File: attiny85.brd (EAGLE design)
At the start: 88.3 x 50.2 mm, 9 parts, among them U2 ATTINY85V-10SU

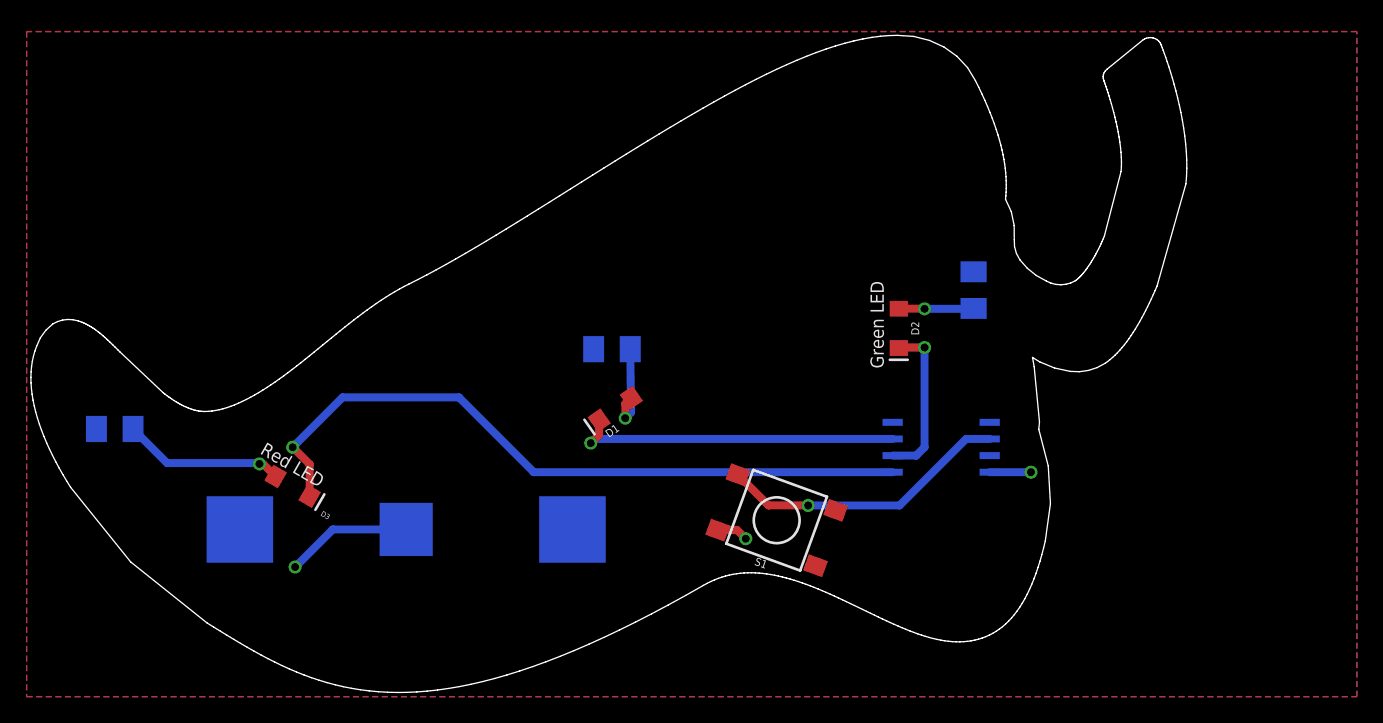
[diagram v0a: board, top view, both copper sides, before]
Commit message: Flipping to output through the attiny
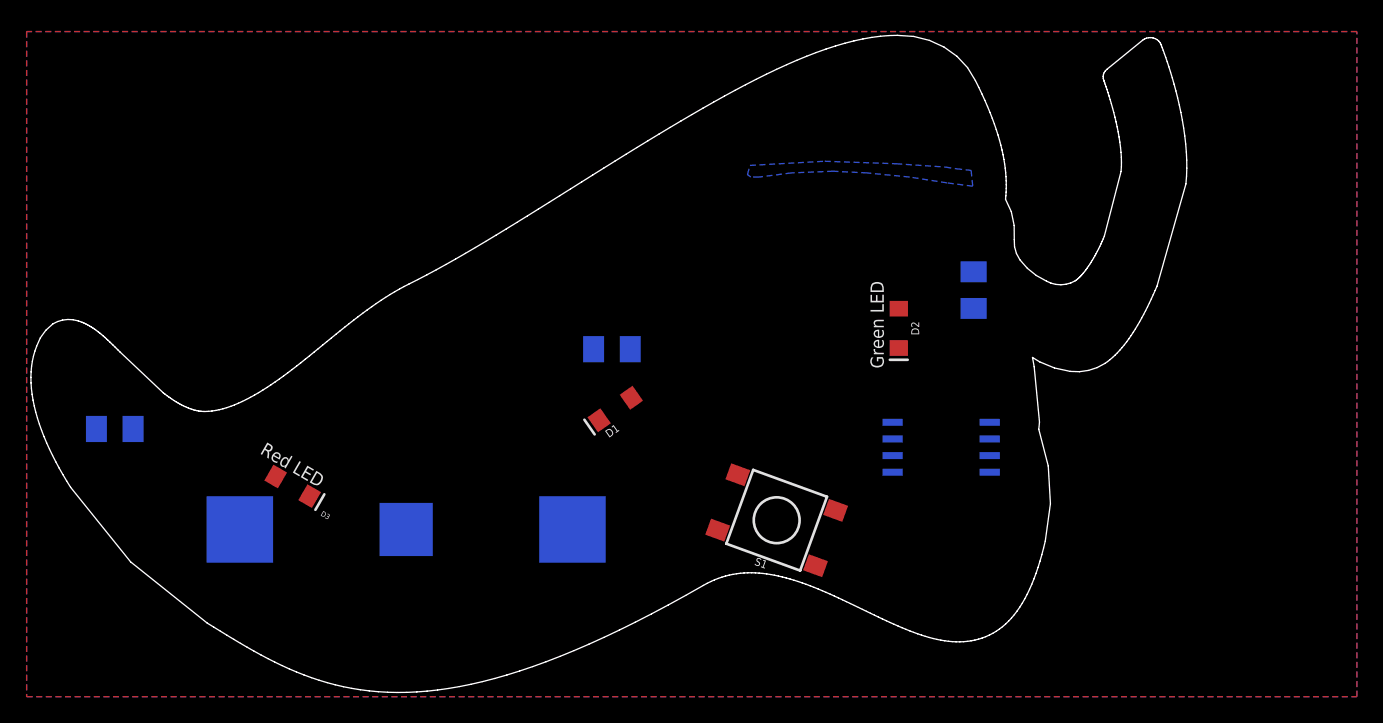
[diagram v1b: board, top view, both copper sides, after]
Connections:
- removed net VCC: BAT1.+$1, BAT1.+$2, R1.1, R2.1, R3.1, S1.B2, U2.8
- new net N$8: R3.1, U2.2
- net GND: now also D1.C, D2.C, D3.C
- net N$3: now also BAT1.+$1, BAT1.+$2, S1.B2, U2.8; no longer D3.C, U2.5
- net N$4: now also R1.1; no longer D2.C
- net N$6: now also S1.A2, U2.5; no longer D1.C, U2.7
- net N$7: now also R2.1, U2.7; no longer S1.A2, U2.2
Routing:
- net N$3: track 54.0 -> 0.00 mm, vias 1 -> 0
- net N$6: track 25.2 -> 0.00 mm, vias 1 -> 0
- net N$7: track 22.3 -> 0.00 mm, vias 1 -> 0
- net GND: track 12.8 -> 0.00 mm, vias 2 -> 0
- net N$1: track 12.4 -> 0.00 mm, vias 1 -> 0
- net N$4: track 12.3 -> 0.00 mm, vias 1 -> 0
- net N$5: track 7.21 -> 0.00 mm, vias 1 -> 0
- net N$2: track 5.73 -> 0.00 mm, vias 1 -> 0
- net VCC: track 2.42 -> 0.00 mm, vias 1 -> 0
- added copper zone on layer 16, net NTOUCH
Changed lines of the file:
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@@
 <contactref element="R2" pad="2"/>
 <contactref element="D2" pad="A"/>
-<wire x1="66.6115" y1="29.6305" x2="68.57225" y2="29.6305" width="0.6096" layer="1"/>
-<wire x1="68.57225" y1="29.6305" x2="68.58" y2="29.62275" width="0.6096" layer="1"/>
-<via x="68.58" y="29.62275" extent="1-16" drill="0.6"/>
-<wire x1="68.58" y1="29.62275" x2="72.29775" y2="29.62275" width="0.6096" layer="16"/>
-<wire x1="72.29775" y1="29.62275" x2="72.3265" y2="29.6515" width="0.6096" layer="16"/>
+<wire x1="66.6115" y1="29.6305" x2="72.3265" y2="29.6515" width="0" layer="19" extent="1-16"/>
 </signal>
 <signal name="VCC">
-<contactref element="R2" pad="1"/>
-<contactref element="BAT1" pad="+$1"/>
-<contactref element="BAT1" pad="+$2"/>
-<contactref element="U2" pad="8"/>
-<contactref element="R3" pad="1"/>
-<contactref element="R1" pad="1"/>
-<contactref element="S1" pad="B2"/>
-<polygon width="0.4064" layer="16">
+<polygon width="0.4064" layer="16" rank="6">
 <vertex x="0" y="0"/>
 <vertex x="101.6" y="0"/>
@@
 <vertex x="0" y="50.8"/>
 </polygon>
-<wire x1="52.781228125" y1="12.72185" x2="54.27065" y2="12.72185" width="0.6096" layer="1"/>
-<wire x1="54.27065" y1="12.72185" x2="54.9275" y2="12.065" width="0.6096" layer="1"/>
-<via x="54.9275" y="12.065" extent="1-16" drill="0.6"/>
 </signal>
 <signal name="GND">
@@
 <vertex x="0" y="50.8"/>
 </polygon>
-<wire x1="28.9885" y1="12.7725" x2="23.377" y2="12.7725" width="0.6096" layer="16"/>
-<wire x1="23.377" y1="12.7725" x2="20.5105" y2="9.906" width="0.6096" layer="16"/>
-<via x="20.5105" y="9.906" extent="1-16" drill="0.6"/>
-<wire x1="73.5584" y1="17.145" x2="76.708" y2="17.145" width="0.6096" layer="16"/>
-<via x="76.708" y="17.145" extent="1-16" drill="0.6"/>
+<contactref element="D1" pad="C"/>
+<contactref element="D3" pad="C"/>
+<contactref element="D2" pad="C"/>
+<wire x1="73.5584" y1="17.145" x2="66.6115" y2="26.6305" width="0" layer="19" extent="1-16"/>
+<wire x1="43.729271875" y1="21.110634375" x2="66.6115" y2="26.6305" width="0" layer="19" extent="1-1"/>
+<wire x1="28.9885" y1="12.7725" x2="43.729271875" y2="21.110634375" width="0" layer="19" extent="1-16"/>
+<wire x1="21.6190375" y1="15.3155" x2="28.9885" y2="12.7725" width="0" layer="19" extent="1-16"/>
 </signal>
 <signal name="N$1">
 <contactref element="R3" pad="2"/>
 <contactref element="D3" pad="A"/>
-<wire x1="19.020959375" y1="16.8155" x2="18.056459375" y2="17.78" width="0.6096" layer="1"/>
-<wire x1="18.056459375" y1="17.78" x2="17.78" y2="17.78" width="0.6096" layer="1"/>
-<via x="17.78" y="17.78" extent="1-16" drill="0.6"/>
-<wire x1="17.78" y1="17.78" x2="17.7165" y2="17.8435" width="0.6096" layer="16"/>
-<wire x1="17.7165" y1="17.8435" x2="10.7345" y2="17.8435" width="0.6096" layer="16"/>
-<wire x1="10.7345" y1="17.8435" x2="8.131" y2="20.447" width="0.6096" layer="16"/>
-</signal>
-<signal name="N$3">
-<contactref element="D3" pad="C"/>
-<contactref element="U2" pad="5"/>
-<wire x1="38.735" y1="17.145" x2="33.02" y2="22.86" width="0.6096" layer="16"/>
-<wire x1="33.02" y1="22.86" x2="24.13" y2="22.86" width="0.6096" layer="16"/>
-<wire x1="24.13" y1="22.86" x2="20.32" y2="19.05" width="0.6096" layer="16"/>
-<via x="20.32" y="19.05" extent="1-16" drill="0.6"/>
-<wire x1="20.32" y1="19.05" x2="21.6190375" y2="17.7509625" width="0.6096" layer="1"/>
-<wire x1="21.6190375" y1="17.7509625" x2="21.6190375" y2="15.3155" width="0.6096" layer="1"/>
-<wire x1="66.1416" y1="17.145" x2="38.735" y2="17.145" width="0.6096" layer="16"/>
-</signal>
-<signal name="N$4">
-<contactref element="U2" pad="6"/>
-<contactref element="D2" pad="C"/>
-<wire x1="66.1416" y1="18.415" x2="67.945" y2="18.415" width="0.6096" layer="16"/>
-<wire x1="67.945" y1="18.415" x2="68.58" y2="19.05" width="0.6096" layer="16"/>
-<wire x1="68.58" y1="19.05" x2="68.58" y2="26.67" width="0.6096" layer="16"/>
-<via x="68.58" y="26.67" extent="1-16" drill="0.6"/>
-<wire x1="68.58" y1="26.67" x2="66.651" y2="26.67" width="0.6096" layer="1"/>
-<wire x1="66.651" y1="26.67" x2="66.6115" y2="26.6305" width="0.6096" layer="1"/>
+<wire x1="8.131" y1="20.447" x2="19.020959375" y2="16.8155" width="0" layer="19" extent="1-16"/>
 </signal>
 <signal name="N$5">
 <contactref element="R1" pad="2"/>
 <contactref element="D1" pad="A"/>
-<wire x1="46.186725" y1="22.8313625" x2="45.72" y2="22.3646375" width="0.6096" layer="1"/>
-<wire x1="45.72" y1="22.3646375" x2="45.72" y2="21.2725" width="0.6096" layer="1"/>
-<via x="45.72" y="21.2725" extent="1-16" drill="0.6"/>
-<wire x1="45.72" y1="21.2725" x2="46.1645" y2="21.717" width="0.6096" layer="16"/>
-<wire x1="46.1645" y1="21.717" x2="46.104" y2="26.543" width="0.6096" layer="16"/>
+<wire x1="46.186725" y1="22.8313625" x2="46.104" y2="26.543" width="0" layer="19" extent="1-16"/>
+</signal>
+<signal name="NTOUCH">
+<polygon width="0.1524" layer="16">
+<vertex x="55.245" y="40.5765"/>
+<vertex x="60.96" y="40.894"/>
+<vertex x="66.421" y="40.7035"/>
+<vertex x="70.1675" y="40.4495"/>
+<vertex x="70.993" y="40.3225"/>
+<vertex x="72.136" y="40.1955"/>
+<vertex x="72.263" y="38.989"/>
+<vertex x="70.2945" y="39.243"/>
+<vertex x="67.437" y="39.6875"/>
+<vertex x="64.1985" y="40.005"/>
+<vertex x="61.595" y="40.132"/>
+<vertex x="58.42" y="40.005"/>
+<vertex x="55.9435" y="39.6875"/>
+<vertex x="55.3085" y="39.6875"/>
+<vertex x="55.0545" y="39.878"/>
+</polygon>
+</signal>
+<signal name="N$3">
+<contactref element="BAT1" pad="+$1"/>
+<contactref element="BAT1" pad="+$2"/>
+<contactref element="U2" pad="8"/>
+<contactref element="S1" pad="B2"/>
+<wire x1="52.781228125" y1="12.72185" x2="66.1416" y2="20.955" width="0" layer="19" extent="1-16"/>
+<wire x1="41.6885" y1="12.7725" x2="52.781228125" y2="12.72185" width="0" layer="19" extent="1-16"/>
+<wire x1="16.2885" y1="12.7725" x2="41.6885" y2="12.7725" width="0" layer="19" extent="16-16"/>
 </signal>
 <signal name="N$6">
-<contactref element="D1" pad="C"/>
-<contactref element="U2" pad="7"/>
-<wire x1="43.729271875" y1="21.110634375" x2="43.729271875" y2="19.980271875" width="0.6096" layer="1"/>
-<wire x1="43.729271875" y1="19.980271875" x2="43.08475" y2="19.3675" width="0.6096" layer="1"/>
-<via x="43.08475" y="19.3675" extent="1-16" drill="0.6"/>
-<wire x1="66.1416" y1="19.685" x2="43.40225" y2="19.685" width="0.6096" layer="16"/>
-<wire x1="43.40225" y1="19.685" x2="43.08475" y2="19.3675" width="0.6096" layer="16"/>
+<contactref element="U2" pad="5"/>
+<contactref element="S1" pad="A2"/>
+<wire x1="54.32031875" y1="16.95046875" x2="66.1416" y2="17.145" width="0" layer="19" extent="1-16"/>
+</signal>
+<signal name="N$4">
+<contactref element="U2" pad="6"/>
+<contactref element="R1" pad="1"/>
+<wire x1="43.304" y1="26.543" x2="66.1416" y2="18.415" width="0" layer="19" extent="16-16"/>
 </signal>
 <signal name="N$7">
-<contactref element="S1" pad="A2"/>
+<contactref element="U2" pad="7"/>
+<contactref element="R2" pad="1"/>
+<wire x1="66.1416" y1="19.685" x2="72.3265" y2="32.4515" width="0" layer="19" extent="16-16"/>
+</signal>
+<signal name="N$8">
 <contactref element="U2" pad="2"/>
-<wire x1="73.5584" y1="19.685" x2="71.755" y2="19.685" width="0.6096" layer="16"/>
-<via x="59.69" y="14.605" extent="1-16" drill="0.6"/>
-<wire x1="59.69" y1="14.605" x2="56.6657875" y2="14.605" width="0.6096" layer="1"/>
-<wire x1="56.6657875" y1="14.605" x2="54.32031875" y2="16.95046875" width="0.6096" layer="1"/>
-<wire x1="71.755" y1="19.685" x2="66.675" y2="14.605" width="0.6096" layer="16"/>
-<wire x1="66.675" y1="14.605" x2="59.69" y2="14.605" width="0.6096" layer="16"/>
+<contactref element="R3" pad="1"/>
+<wire x1="5.331" y1="20.447" x2="73.5584" y2="19.685" width="0" layer="19" extent="16-16"/>
 </signal>
 </signals>
